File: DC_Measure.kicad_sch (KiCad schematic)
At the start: 37 parts, among them U1 LM2904

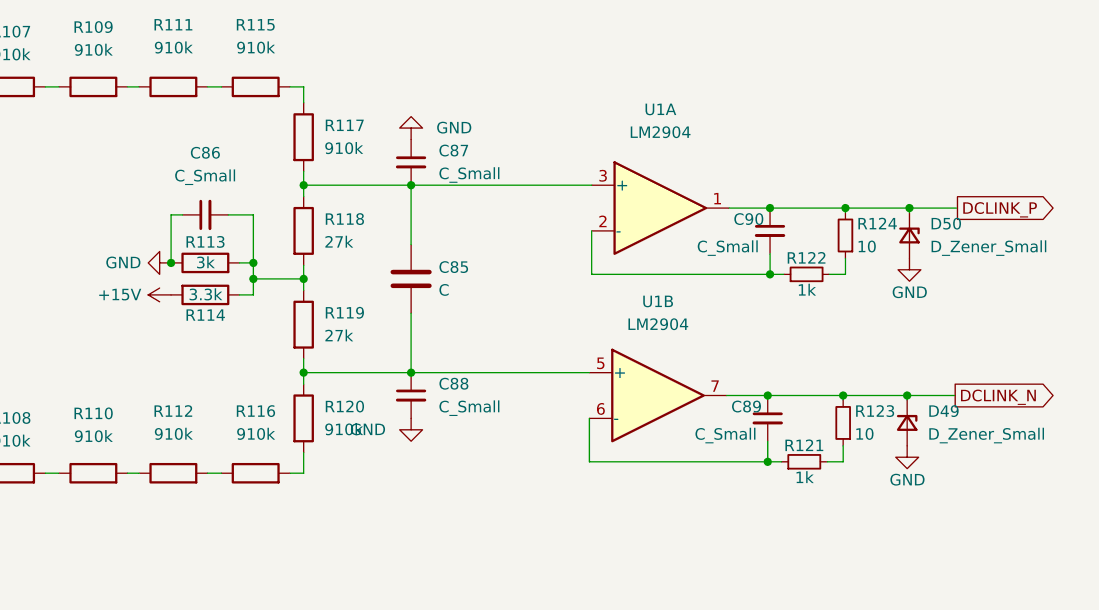
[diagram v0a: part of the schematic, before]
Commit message: Добавил названия элементов в схеме
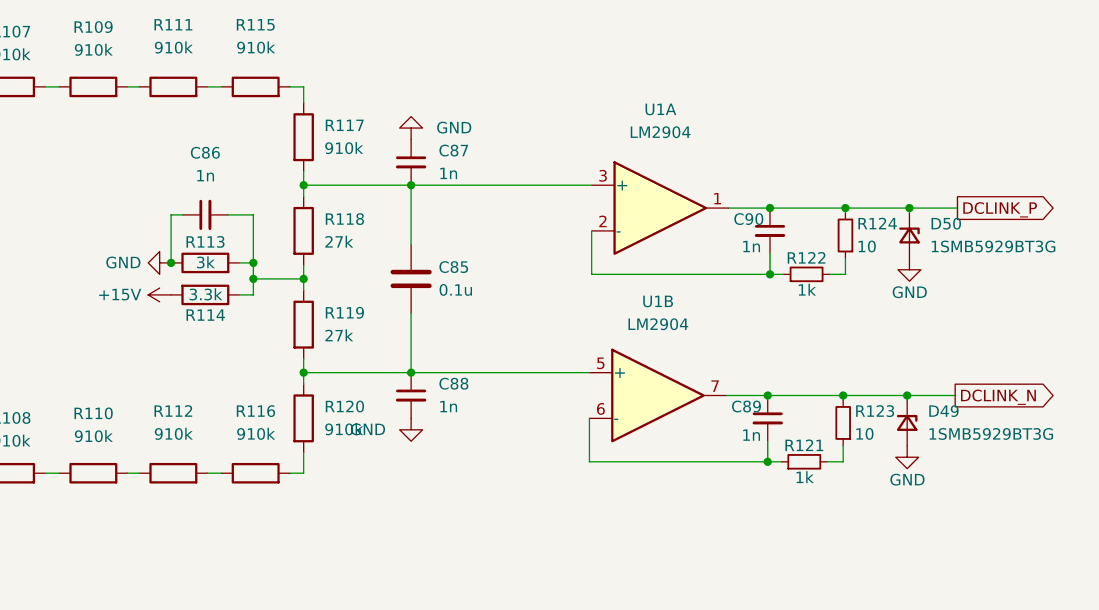
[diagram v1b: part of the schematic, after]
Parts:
- C85: value C -> 0.1u
- C86, C87, C88, C89, C90: value C_Small -> 1n
- D49, D50: value D_Zener_Small -> 1SMB5929BT3G
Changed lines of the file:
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@@
       (effects (font (size 1.27 1.27)) (justify left))
     )
-    (property "Value" "C_Small" (id 1) (at 144.018 99.568 0)
+    (property "Value" "1n" (id 1) (at 149.225 99.695 0)
       (effects (font (size 1.27 1.27)) (justify left))
     )
@@
       (effects (font (size 1.27 1.27)) (justify left))
     )
-    (property "Value" "D_Zener_Small" (id 1) (at 169.926 99.5679 90)
+    (property "Value" "1SMB5929BT3G" (id 1) (at 169.926 99.5679 90)
       (effects (font (size 1.27 1.27)) (justify left))
     )
@@
       (effects (font (size 1.27 1.27)) (justify left))
     )
-    (property "Value" "C_Small" (id 1) (at 115.57 96.5262 0)
+    (property "Value" "1n" (id 1) (at 115.57 96.5262 0)
       (effects (font (size 1.27 1.27)) (justify left))
     )
@@
     (in_bom yes) (on_board yes) (fields_autoplaced)
     (property "Reference" "C86" (id 0) (at 89.6683 68.326 90))
-    (property "Value" "C_Small" (id 1) (at 89.6683 70.866 90))
+    (property "Value" "1n" (id 1) (at 89.6683 70.866 90))
     (property "Footprint" "Capacitor_SMD:C_0805_2012Metric_Pad1.18x1.45mm_HandSolder" (id 2) (at 89.662 75.184 0)
       (effects (font (size 1.27 1.27)) hide)
@@
       (effects (font (size 1.27 1.27)) (justify left))
     )
-    (property "Value" "C_Small" (id 1) (at 115.57 70.6182 0)
+    (property "Value" "1n" (id 1) (at 115.57 70.6182 0)
       (effects (font (size 1.27 1.27)) (justify left))
     )
@@
       (effects (font (size 1.27 1.27)) (justify left))
     )
-    (property "Value" "C_Small" (id 1) (at 144.272 78.74 0)
+    (property "Value" "1n" (id 1) (at 149.225 78.74 0)
       (effects (font (size 1.27 1.27)) (justify left))
     )
@@
       (effects (font (size 1.27 1.27)) (justify left))
     )
-    (property "Value" "C" (id 1) (at 115.57 83.5659 0)
+    (property "Value" "0.1u" (id 1) (at 115.57 83.5659 0)
       (effects (font (size 1.27 1.27)) (justify left))
     )
@@
       (effects (font (size 1.27 1.27)) (justify left))
     )
-    (property "Value" "D_Zener_Small" (id 1) (at 170.18 78.7399 90)
-      (effects (font (size 1.27 1.27)) (justify left))
-    )
+    (property "Value" "1SMB5929BT3G" (id 1) (at 170.18 78.7399 90)
+      (effects (font (size 1.27 1.27)) (justify left))
+    )

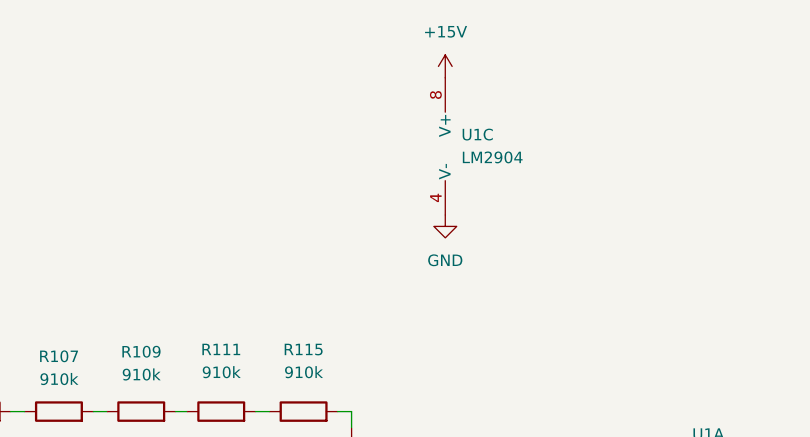
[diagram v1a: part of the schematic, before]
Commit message: REV2.1 - добавил конденсатор по питанию измерения DC
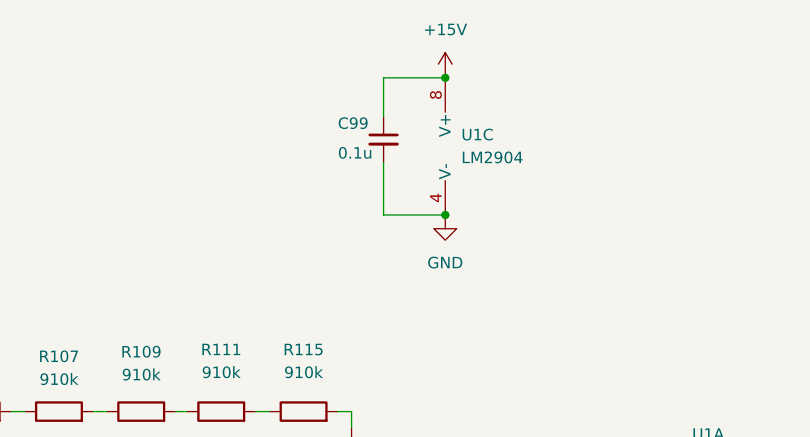
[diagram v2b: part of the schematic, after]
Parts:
- added C99: 0.1u, Capacitor_SMD:C_0805_2012Metric_Pad1.18x1.45mm_HandSolder, symbol Device:C_Small
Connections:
- net +15V: now also C99.1
- net GND: now also C99.2
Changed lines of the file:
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@@
   (junction (at 94.996 82.296) (diameter 0) (color 0 0 0 0)
   )
+  (junction (at 110.998 23.876) (diameter 0) (color 0 0 0 0)
+  )
   (junction (at 85.852 80.518) (diameter 0) (color 0 0 0 0)
   )
@@
   (junction (at 152.4 81.788) (diameter 0) (color 0 0 0 0)
   )
+  (junction (at 110.998 39.116) (diameter 0) (color 0 0 0 0)
+  )
   (junction (at 152.146 102.616) (diameter 0) (color 0 0 0 0)
   )
@@
     (stroke (width 0) (type default) (color 0 0 0 0))
   )
+  (wire (pts (xy 110.998 23.622) (xy 110.998 23.876))
+    (stroke (width 0) (type default) (color 0 0 0 0))
+  )
   (wire (pts (xy 132.588 76.962) (xy 132.588 81.788))
     (stroke (width 0) (type default) (color 0 0 0 0))
@@
     (stroke (width 0) (type default) (color 0 0 0 0))
   )
+  (wire (pts (xy 104.14 28.194) (xy 104.14 23.876))
+    (stroke (width 0) (type default) (color 0 0 0 0))
+  )
+  (wire (pts (xy 104.14 23.876) (xy 110.998 23.876))
+    (stroke (width 0) (type default) (color 0 0 0 0))
+  )
   (wire (pts (xy 160.528 102.616) (xy 158.75 102.616))
     (stroke (width 0) (type default) (color 0 0 0 0))
@@
     (stroke (width 0) (type default) (color 0 0 0 0))
   )
+  (wire (pts (xy 104.14 39.116) (xy 110.998 39.116))
+    (stroke (width 0) (type default) (color 0 0 0 0))
+  )
   (wire (pts (xy 100.584 101.6) (xy 100.584 103.886))
     (stroke (width 0) (type default) (color 0 0 0 0))
@@
   )
   (wire (pts (xy 89.916 60.96) (xy 91.44 60.96))
+    (stroke (width 0) (type default) (color 0 0 0 0))
+  )
+  (wire (pts (xy 110.998 39.37) (xy 110.998 39.116))
+    (stroke (width 0) (type default) (color 0 0 0 0))
+  )
+  (wire (pts (xy 104.14 33.274) (xy 104.14 39.116))
     (stroke (width 0) (type default) (color 0 0 0 0))
   )
@@
     (pin "2")
   )
-  (symbol (lib_id "power:GND") (at 110.998 39.116 0) (unit 1)
-    (in_bom yes) (on_board yes) (fields_autoplaced)
-    (property "Reference" "#PWR05" (id 0) (at 110.998 45.466 0)
-      (effects (font (size 1.27 1.27)) hide)
-    )
-    (property "Value" "GND" (id 1) (at 110.998 44.196 0))
-    (property "Footprint" "" (id 2) (at 110.998 39.116 0)
-      (effects (font (size 1.27 1.27)) hide)
-    )
-    (property "Datasheet" "" (id 3) (at 110.998 39.116 0)
+  (symbol (lib_id "power:GND") (at 110.998 39.37 0) (unit 1)
+    (in_bom yes) (on_board yes) (fields_autoplaced)
+    (property "Reference" "#PWR05" (id 0) (at 110.998 45.72 0)
+      (effects (font (size 1.27 1.27)) hide)
+    )
+    (property "Value" "GND" (id 1) (at 110.998 44.45 0))
+    (property "Footprint" "" (id 2) (at 110.998 39.37 0)
+      (effects (font (size 1.27 1.27)) hide)
+    )
+    (property "Datasheet" "" (id 3) (at 110.998 39.37 0)
       (effects (font (size 1.27 1.27)) hide)
     )
@@
     (pin "8")
   )
+  (symbol (lib_id "Device:C_Small") (at 104.14 30.734 0) (unit 1)
+    (in_bom yes) (on_board yes)
+    (property "Reference" "C99" (id 0) (at 99.06 28.956 0)
+      (effects (font (size 1.27 1.27)) (justify left))
+    )
+    (property "Value" "0.1u" (id 1) (at 99.06 32.258 0)
+      (effects (font (size 1.27 1.27)) (justify left))
+    )
+    (property "Footprint" "Capacitor_SMD:C_0805_2012Metric_Pad1.18x1.45mm_HandSolder" (id 2) (at 104.14 30.734 0)
+      (effects (font (size 1.27 1.27)) hide)
+    )
+    (property "Datasheet" "~" (id 3) (at 104.14 30.734 0)
+      (effects (font (size 1.27 1.27)) hide)
+    )
+    (pin "1")
+    (pin "2")
+  )
   (symbol (lib_id "Device:R") (at 95.25 103.886 90) (unit 1)
     (in_bom yes) (on_board yes) (fields_autoplaced)
@@
     (pin "2")
   )
-  (symbol (lib_id "power:+15V") (at 110.998 23.876 0) (unit 1)
-    (in_bom yes) (on_board yes) (fields_autoplaced)
-    (property "Reference" "#PWR04" (id 0) (at 110.998 27.686 0)
-      (effects (font (size 1.27 1.27)) hide)
-    )
-    (property "Value" "+15V" (id 1) (at 110.998 18.796 0))
-    (property "Footprint" "" (id 2) (at 110.998 23.876 0)
-      (effects (font (size 1.27 1.27)) hide)
-    )
-    (property "Datasheet" "" (id 3) (at 110.998 23.876 0)
-      (effects (font (size 1.27 1.27)) hide)
-    )
+  (symbol (lib_id "power:+15V") (at 110.998 23.622 0) (unit 1)
+    (in_bom yes) (on_board yes) (fields_autoplaced)
+    (property "Reference" "#PWR04" (id 0) (at 110.998 27.432 0)
+      (effects (font (size 1.27 1.27)) hide)
+    )
+    (property "Value" "+15V" (id 1) (at 110.998 18.542 0))
+    (property "Footprint" "" (id 2) (at 110.998 23.622 0)
+      (effects (font (size 1.27 1.27)) hide)
+    )
+    (property "Datasheet" "" (id 3) (at 110.998 23.622 0)
+      (effects (font (size 1.27 1.27)) hide)
+    )
